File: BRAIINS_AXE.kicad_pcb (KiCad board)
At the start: 6 copper layers, 105.5 x 181.1 mm, 298 parts, among them J1 RJ45_Hanrun_HR911105A_Horizon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, J10 Connector 02x01, J2 Conn_01x06, J9 DISP, M1 Fan_4pin, M2 Fan_4pin, Q1 BSS138, Q2 BSS138, SW1 SW_Omron_B3F-315x, U1 TMP102xxDRL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

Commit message: sch_ should be ready
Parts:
- removed JP1: SolderJumper_2_Open, Jumper:SolderJumper-2_P1.3mm_Open_RoundedPad1.0x1.5mm
- removed U30: T-Display-S3, myfootprints:T-Display-S3
- added C102: 10µ/25V, Capacitor_SMD:C_0805_2012Metric, F.Cu at (20.6, 94.0)
- added C151: 10n, Capacitor_SMD:C_0805_2012Metric, F.Cu at (20.6, 97.0)
- added C152: 22µ/16V, Capacitor_SMD:C_1206_3216Metric, F.Cu at (21.2, 100.2)
- added D6: PMEG4030EP,115, Diode_SMD:D_SOD-128, F.Cu at (22.1, 90.5)
- added L6: 4.7µH/2.3A/2.7A, Inductor_SMD:L_Taiyo-Yuden_NR-50xx, F.Cu at (15.0, 91.7)
- added R156: 33R, Resistor_SMD:R_0603_1608Metric, F.Cu at (103.6, 74.0)
- added R157: 33R, Resistor_SMD:R_0603_1608Metric, F.Cu at (103.7, 76.5)
- added R69: 49.9k, Resistor_SMD:R_0603_1608Metric, F.Cu at (24.8, 93.8)
- added R70: 16.2k, Resistor_SMD:R_0603_1608Metric, F.Cu at (24.8, 96.3)
- added U14: AP3211, Package_TO_SOT_SMD:SOT-23-6, F.Cu at (14.3, 97.4)
- R155: moved to B.Cu
- R32, R34: footprint Resistor_SMD:R_0805_2012Metric -> Resistor_SMD:R_0603_1608Metric
- moved R155 42.1 mm to (123.5, 81.4), turned to 180 degrees
- moved C8 8.05 mm to (93.3, 71.4)
- moved R5 8.05 mm to (78.9, 79.6)
- moved C1 8.05 mm to (82.6, 81.2)
- moved C114 8.05 mm to (88.1, 80.4)
- moved C115 8.05 mm to (86.6, 83.9)
- moved C116 8.05 mm to (89.9, 83.9)
- moved C2 8.05 mm to (80.9, 79.7)
- moved C3 8.05 mm to (90.9, 80.4)
- moved C4 8.05 mm to (94.9, 82.4)
- moved C5 8.05 mm to (93.4, 77.9)
- moved C6 8.05 mm to (93.4, 76.4)
- moved C7 8.05 mm to (93.4, 74.9)
- moved C9 8.05 mm to (85.4, 68.5)
- moved JP2 8.05 mm to (82.7, 68.1)
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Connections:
- A1 pad 14: unconnected-(A1-GPIO10-Pad14) -> Net-(A1-GPIO10)
- A1 pad 15: unconnected-(A1-GPIO11-Pad15) -> Net-(A1-GPIO11)
- A1 pad 16: unconnected-(A1-GPIO12-Pad16) -> /controller/DISP_DC
- A1 pad 17: unconnected-(A1-GPIO13-Pad17) -> /controller/DISP_CSN
- A1 pad 19: unconnected-(A1-GPIO14-Pad19) -> /controller/DISP_RST
- A1 pad 20: unconnected-(A1-GPIO15-Pad20) -> /controller/DISP_ALRT
- C106 pad 1: Net-(JP1-A) -> +5V
- J9 pad 3: unconnected-(J9-Pin_3-Pad3) -> /controller/DISP_ALRT
- J9 pad 4: unconnected-(J9-Pin_4-Pad4) -> /controller/DISP_CSN
- J9 pad 5: unconnected-(J9-Pin_5-Pad5) -> /controller/DISP_DC
- J9 pad 6: unconnected-(J9-Pin_6-Pad6) -> /controller/DISP_RST
- J9 pad 7: unconnected-(J9-Pin_7-Pad7) -> /controller/DISP_MOSI
- J9 pad 8: unconnected-(J9-Pin_8-Pad8) -> /controller/DISP_SCK
- L3 pad 2: Net-(JP1-A) -> +5V
- R32 pad 1: Net-(JP1-A) -> +5V

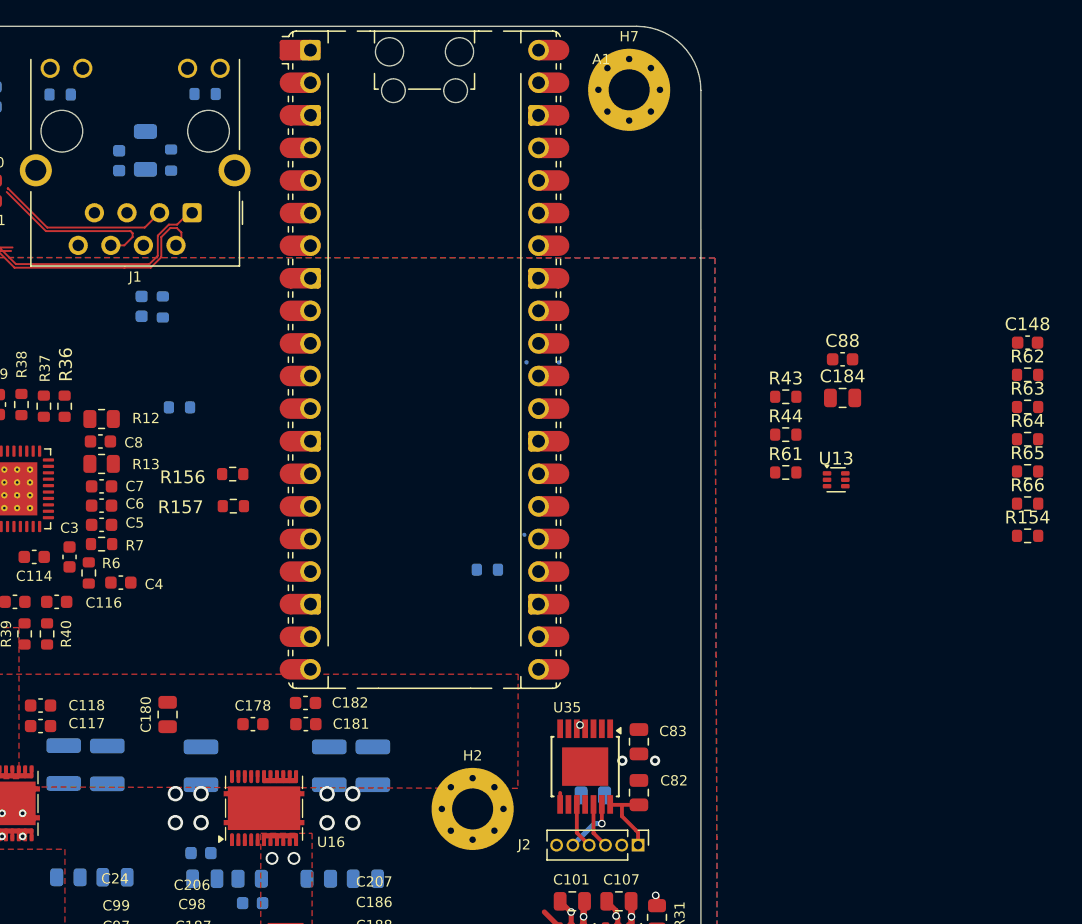
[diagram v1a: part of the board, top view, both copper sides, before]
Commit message: controller resitors in place
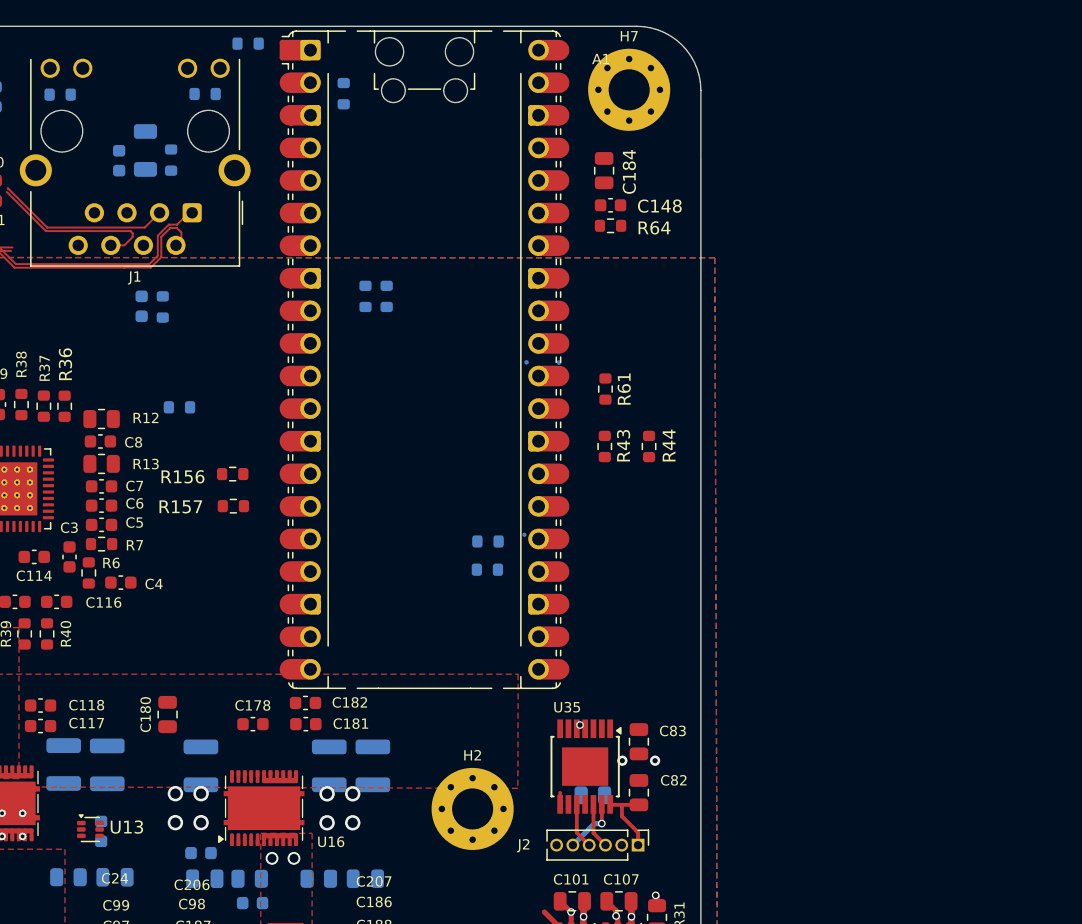
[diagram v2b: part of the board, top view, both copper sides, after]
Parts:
- C88, R154, R62, R63, R65, R66: moved to B.Cu
- moved C88 68.5 mm to (93.3, 101.8), turned to -90 degrees
- moved R62 66.0 mm to (104.8, 40.4)
- moved U13 64.2 mm to (92.5, 101.7)
- moved R63 58.6 mm to (112.2, 44.3), turned to 90 degrees
- moved R65 53.4 mm to (114.0, 60.1), turned to -90 degrees
- moved R66 52.5 mm to (115.6, 60.1), turned to -90 degrees
- moved R154 42.1 mm to (123.5, 79.2), turned to 180 degrees
- moved R64 36.5 mm to (133.1, 54.6)
- moved C148 34.2 mm to (133.1, 53.0)
- moved C184 25.7 mm to (132.6, 50.3), turned to 90 degrees
- moved R61 15.5 mm to (132.7, 67.3), turned to 90 degrees
- moved R43 14.6 mm to (132.6, 71.8), turned to -90 degrees
- moved R44 10.7 mm to (136.1, 71.8), turned to -90 degrees

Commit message: all components placed
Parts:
- C149, C150, D3, D4, JP3, Q1, Q2, R156, R157, R67, R68, R71, R72, R73, R74, R75, R76, R77, R78, R79: moved to B.Cu
- moved R67 87.7 mm to (105.4, 53.7), turned to 90 degrees
- moved U14 55.7 mm to (68.6, 84.9), turned to 90 degrees
- moved L6 54.1 mm to (67.8, 79.6), turned to 90 degrees
- moved C152 52.7 mm to (67.5, 75.2)
- moved C102 52.5 mm to (71.7, 82.2), turned to 90 degrees
- moved C151 46.5 mm to (65.5, 84.9), turned to 90 degrees
- moved R70 46.0 mm to (70.0, 88.0)
- moved D6 42.7 mm to (63.5, 79.9), turned to -90 degrees
- moved R69 42.5 mm to (67.0, 88.0)
- moved R77 34.5 mm to (51.9, 88.7), turned to 180 degrees
- moved D3 33.8 mm to (38.9, 87.6), turned to -90 degrees
- moved R74 32.8 mm to (48.6, 90.3), turned to 180 degrees
- moved C150 31.4 mm to (43.2, 87.5), turned to -90 degrees
- moved R72 31.0 mm to (46.7, 84.8), turned to 180 degrees
- moved D5 30.7 mm to (40.5, 60.6), turned to 180 degrees
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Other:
- board text added: "(3.3V)"
